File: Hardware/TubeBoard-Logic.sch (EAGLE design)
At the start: 35 parts, among them IC1 74HC373DW, IC2 74HC373DW, IC3 74HC85D, IC4 74HC04D, IC5 74HC08D, T1 MPSA42, T2 MPSA42

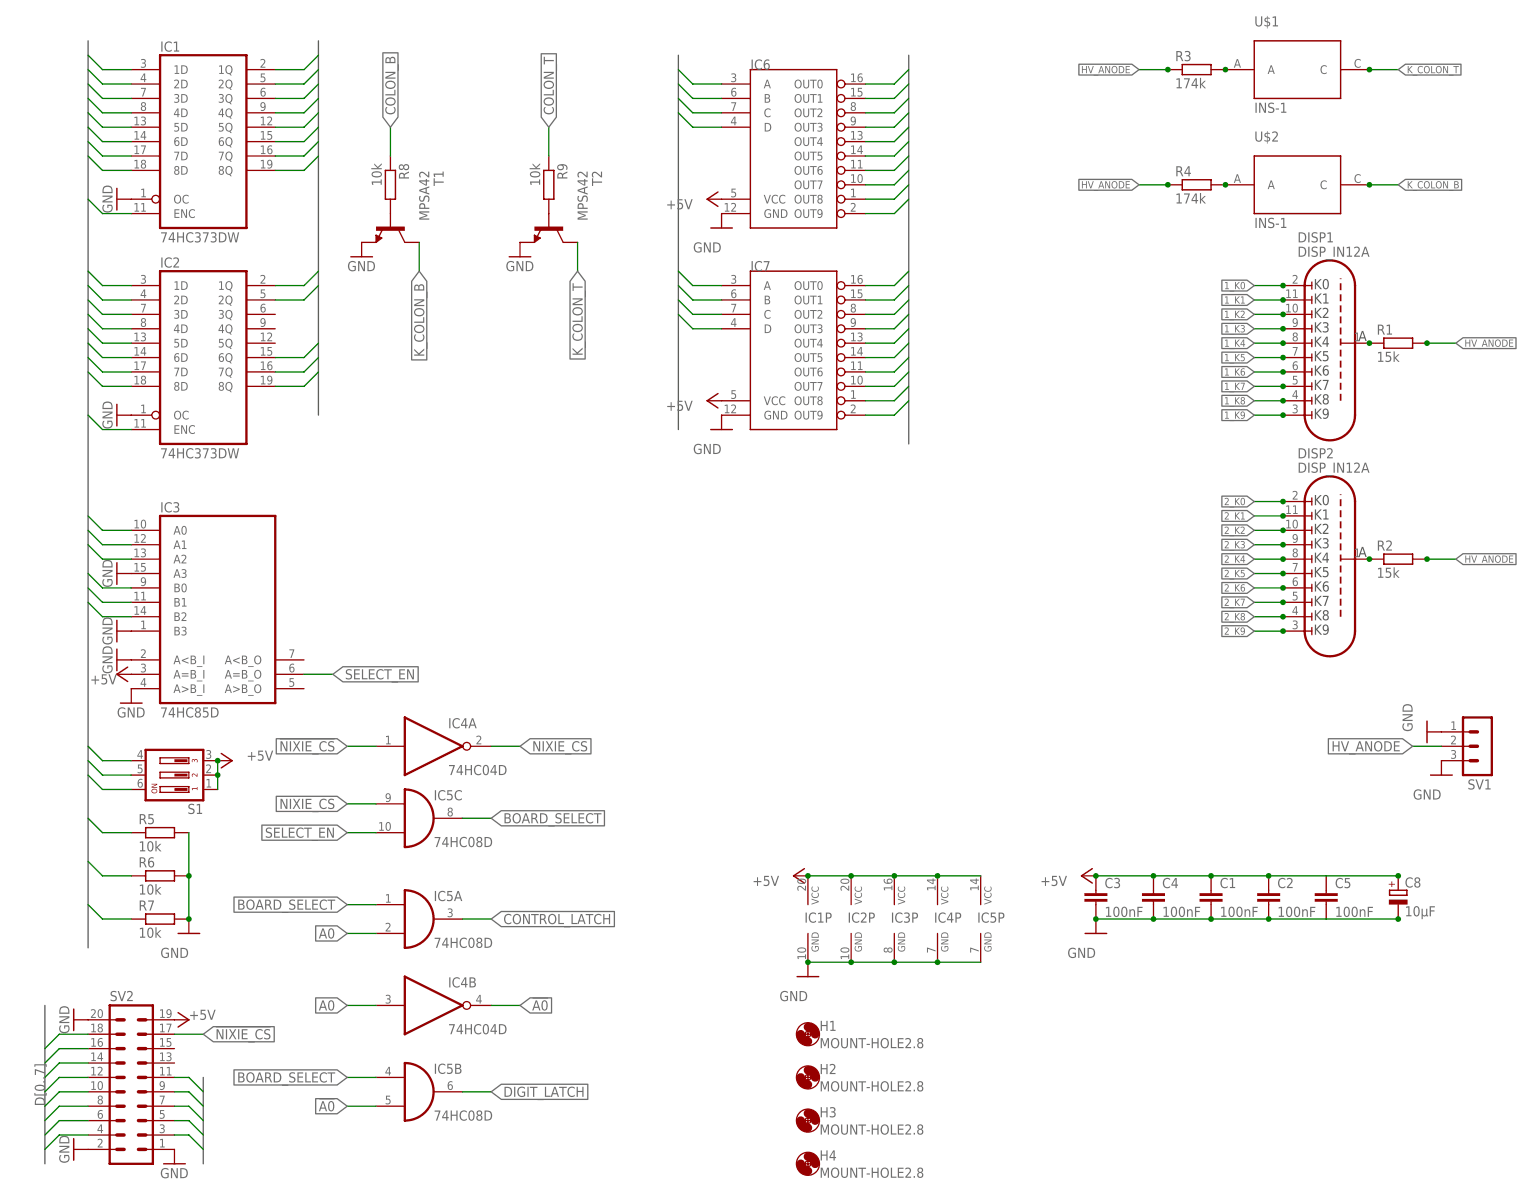
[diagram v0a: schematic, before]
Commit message: separated tubes and logic on two separate boards
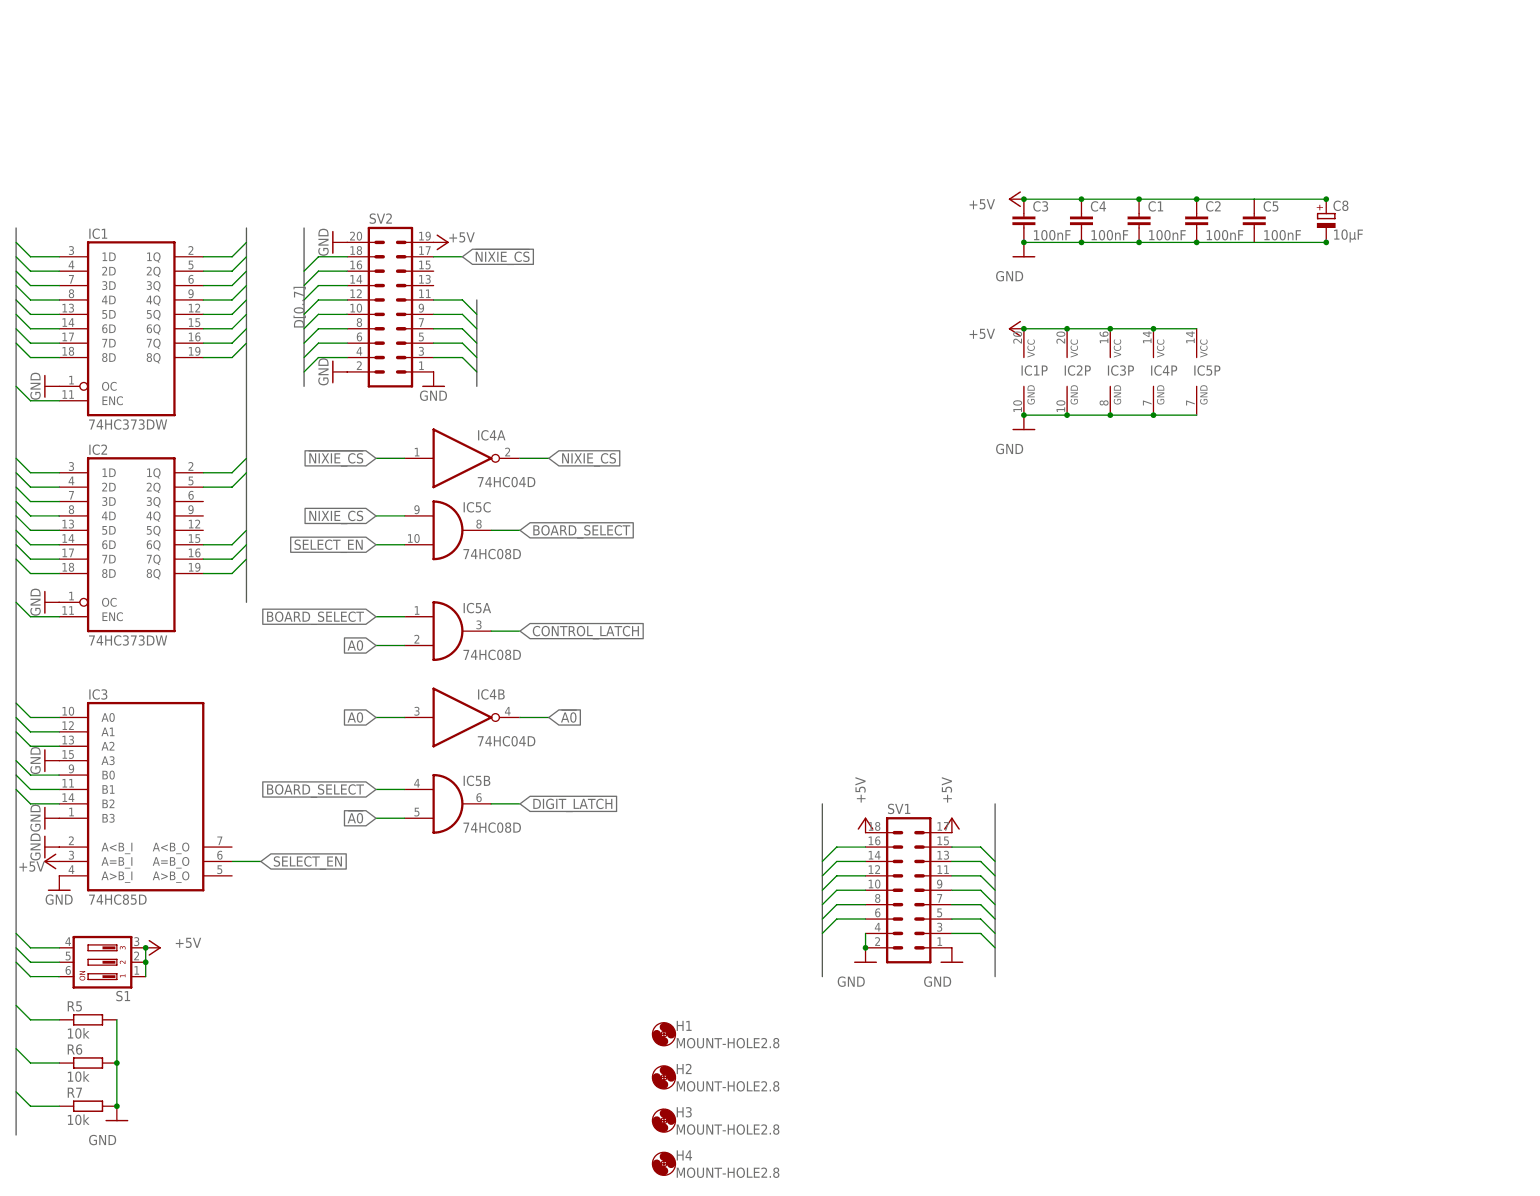
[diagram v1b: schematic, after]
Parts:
- removed DISP1, DISP2: DISP_IN12A, dp_devices:DISP_IN12A
- removed IC6, IC7: (no value), Parts:7441DIL16
- removed R1, R2: 15k, rcl:R-EU_0411/12
- removed R3, R4: 174k, rcl:R-EU_M1206
- removed R8, R9: 10k, rcl:R-EU_R2012
- removed T1, T2: MPSA42, transistor:MPSA42-NPN-TO92-EBC
- removed U$1, U$2: INS-1, Parts:INS-1
- SV1: device con-lstb:MA03-1 -> con-lstb:MA09-2
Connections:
- removed net 1_K0: DISP1.K0, IC6.OUT0
- removed net 1_K1: DISP1.K1, IC6.OUT1
- removed net 1_K2: DISP1.K2, IC6.OUT2
- removed net 1_K3: DISP1.K3, IC6.OUT3
- removed net 1_K4: DISP1.K4, IC6.OUT4
- removed net 1_K5: DISP1.K5, IC6.OUT5
- removed net 1_K6: DISP1.K6, IC6.OUT6
- removed net 1_K7: DISP1.K7, IC6.OUT7
- removed net 1_K8: DISP1.K8, IC6.OUT8
- removed net 1_K9: DISP1.K9, IC6.OUT9
- removed net 2_K0: DISP2.K0, IC7.OUT0
- removed net 2_K1: DISP2.K1, IC7.OUT1
- removed net 2_K2: DISP2.K2, IC7.OUT2
- removed net 2_K3: DISP2.K3, IC7.OUT3
- removed net 2_K4: DISP2.K4, IC7.OUT4
- removed net 2_K5: DISP2.K5, IC7.OUT5
- removed net 2_K6: DISP2.K6, IC7.OUT6
- removed net 2_K7: DISP2.K7, IC7.OUT7
- removed net 2_K8: DISP2.K8, IC7.OUT8
- removed net 2_K9: DISP2.K9, IC7.OUT9
- removed net HV_ANODE: R1.2, R2.2, R3.1, R4.1, SV1.2
- removed net K_COLON_B: T1.C, U$2.C
- removed net K_COLON_T: T2.C, U$1.C
- removed net N$1: DISP1.ANODE, R1.1
- removed net N$2: DISP2.ANODE, R2.1
- removed net N$3: R3.2, U$1.A
- removed net N$4: R4.2, U$2.A
- removed net N$5: R8.2, T1.B
- removed net N$6: R9.2, T2.B
- net +5V: now also SV1.17, SV1.18; no longer IC6.VCC, IC7.VCC
- net COLON_B: now also SV1.8; no longer R8.1
- net COLON_T: now also SV1.6; no longer R9.1
- net DRIVE_HI: now also SV1.3
- net DRIVE_LO: now also SV1.7
- net DRIVE_MED: now also SV1.5
- net GND: now also SV1.2, SV1.4; no longer IC6.GND, IC7.GND, SV1.3, T1.E, T2.E
- net LDIGIT0: now also SV1.16; no longer IC6.A
- net LDIGIT1: now also SV1.14; no longer IC6.B
- net LDIGIT2: now also SV1.12; no longer IC6.C
- net LDIGIT3: now also SV1.10; no longer IC6.D
- net RDIGIT0: now also SV1.15; no longer IC7.A
- net RDIGIT1: now also SV1.13; no longer IC7.B
- net RDIGIT2: now also SV1.11; no longer IC7.C
- net RDIGIT3: now also SV1.9; no longer IC7.D
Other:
- moved on the sheet: C1, C2, C3, C4, C5, C8, H1, H2, H3, H4, IC1, IC1P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

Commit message: routed tube logic board
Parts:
- added SV3: (no value), con-lstb:MA10-2
- added WEED1: WEED, Parts:WEED
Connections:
- net !NIXIE_CS: now also SV3.17
- net +5V: now also SV3.19
- net A0: now also SV3.3
- net A1: now also SV3.5
- net A2: now also SV3.7
- net A3: now also SV3.9
- net A4: now also SV3.11
- net D0: now also SV3.8
- net D1: now also SV3.6
- net D2: now also SV3.4
- net D3: now also SV3.10
- net D4: now also SV3.12
- net D5: now also SV3.14
- net D6: now also SV3.16
- net D7: now also SV3.18
- net GND: now also SV3.1, SV3.2, SV3.20
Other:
- moved on the sheet: SV2

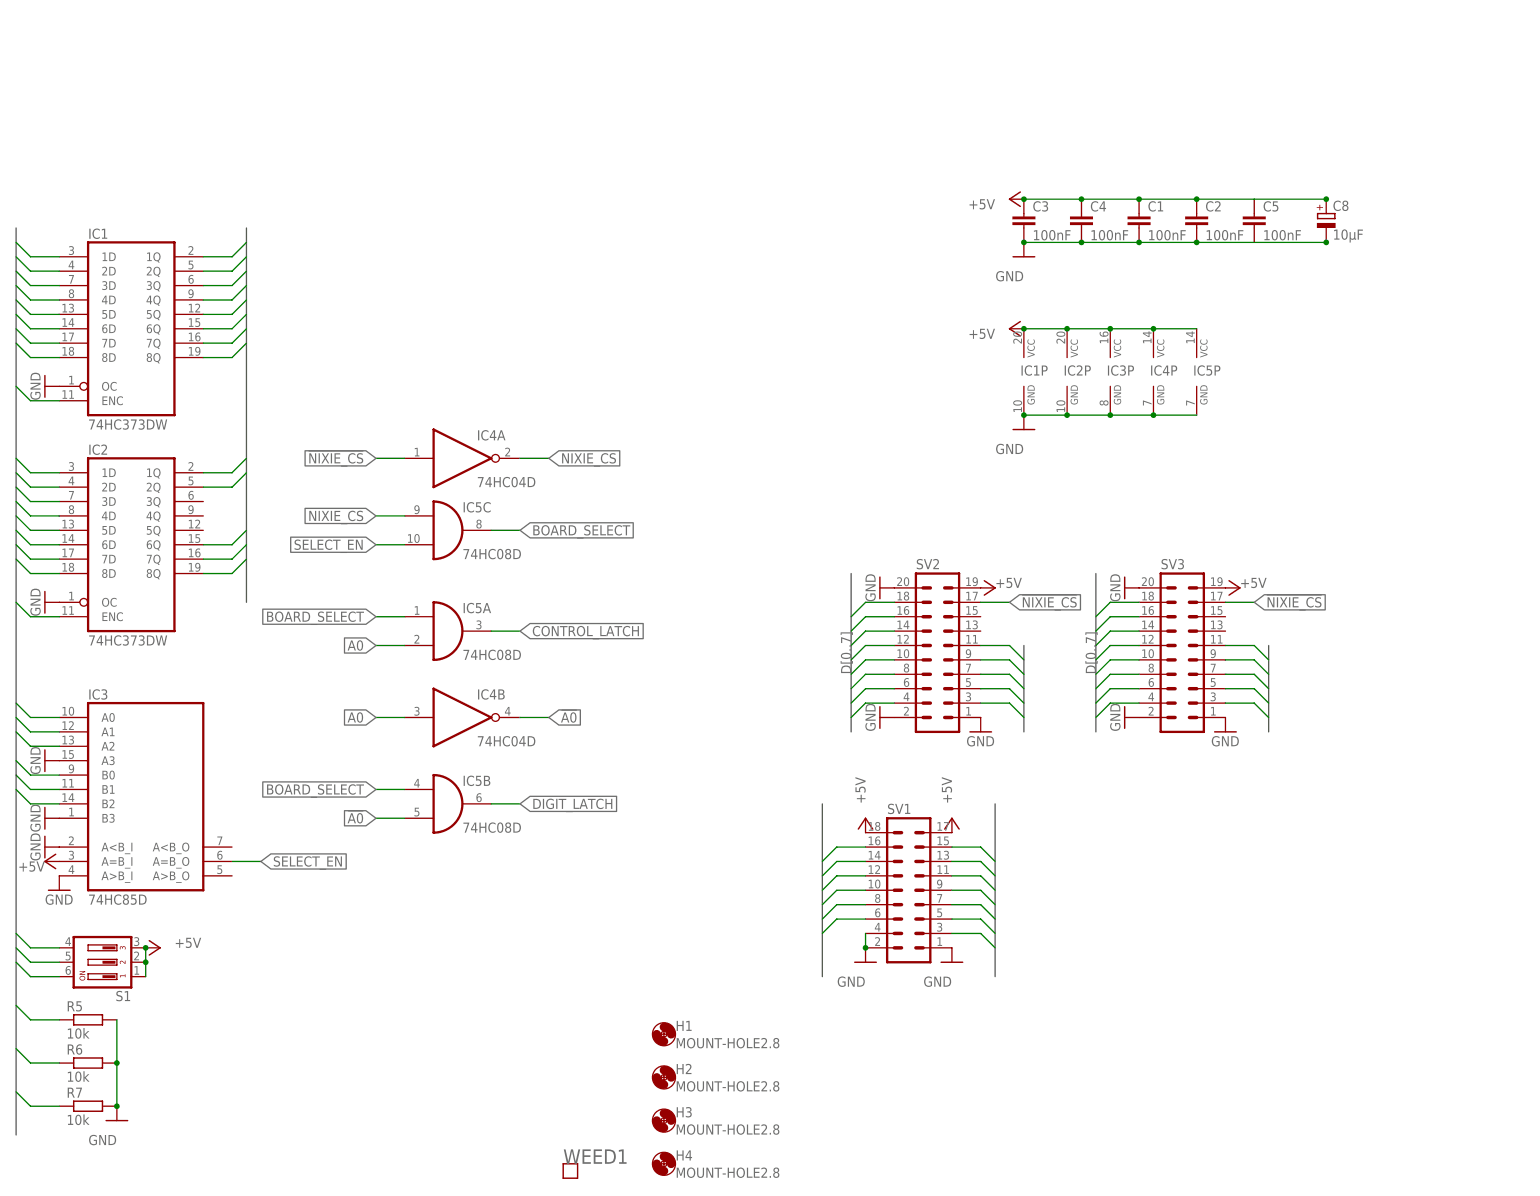
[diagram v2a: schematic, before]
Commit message: added data bus resistors; better reset circuit
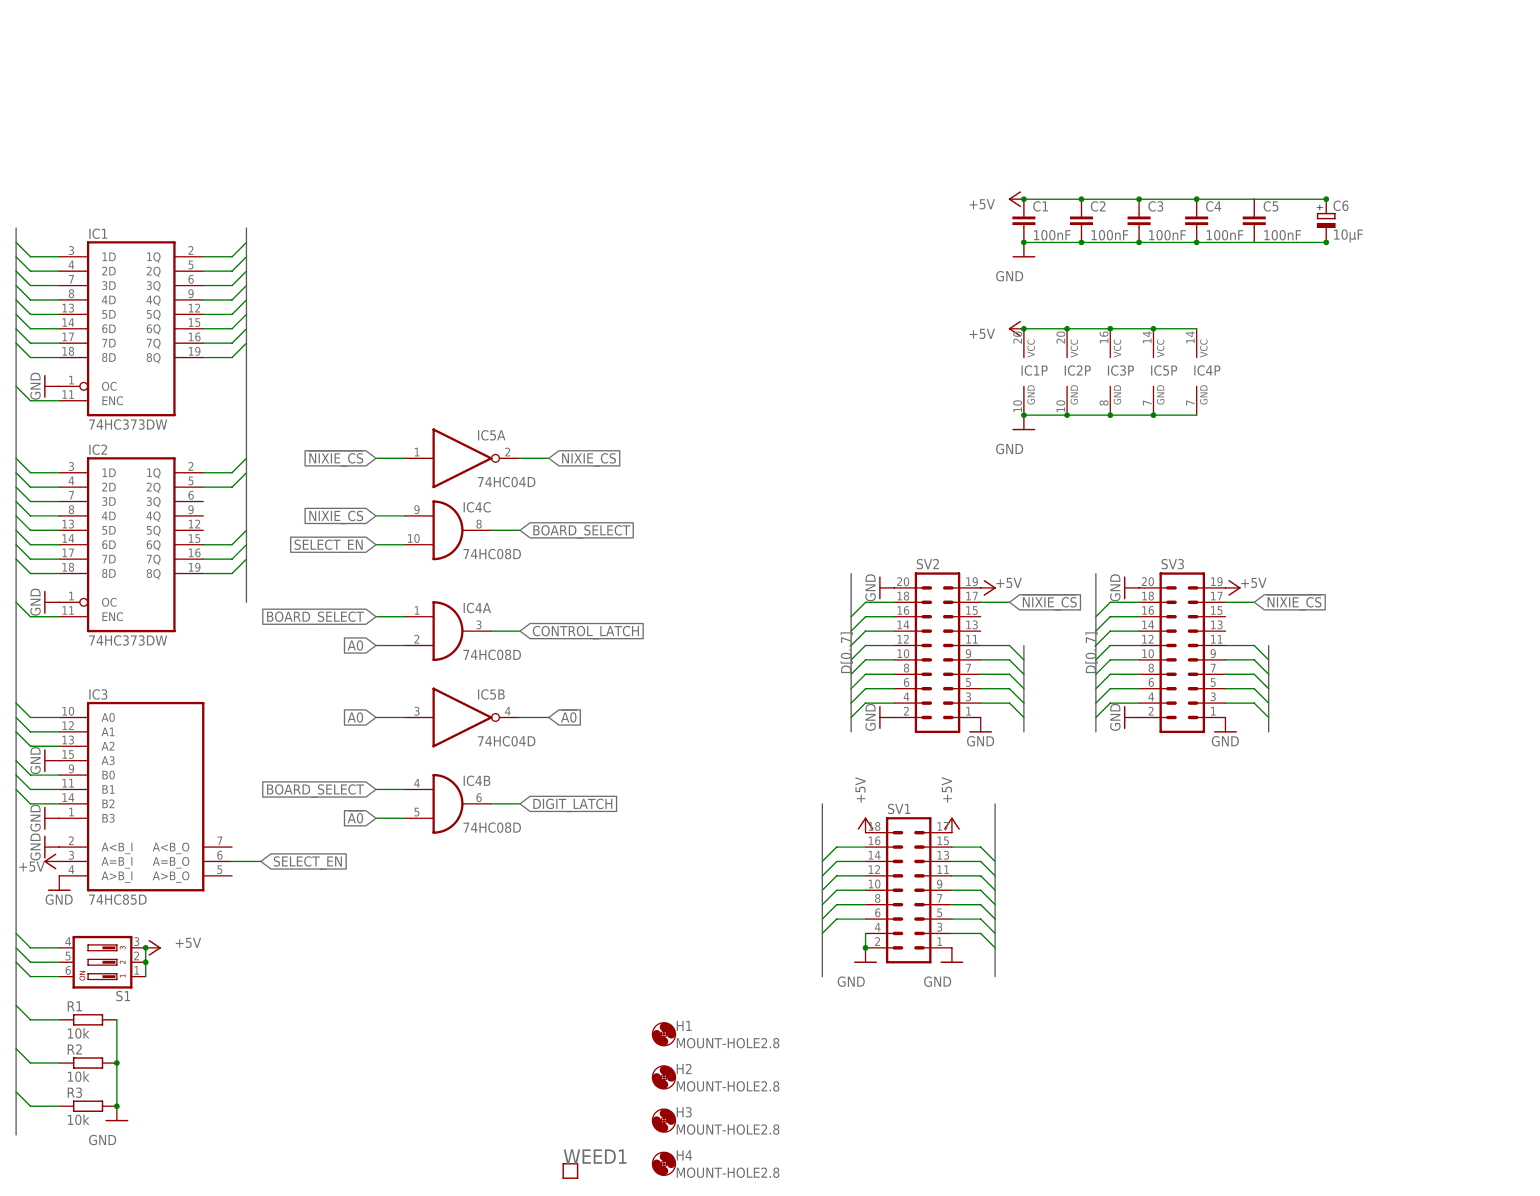
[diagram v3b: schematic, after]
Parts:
- IC4: value 74HC04D -> 74HC08D; device 74xx-eu:74HC04D -> 74xx-eu:74HC08D
- IC5: value 74HC08D -> 74HC04D; device 74xx-eu:74HC08D -> 74xx-eu:74HC04D
- renumbered C8 to C6, R5 to R1, R6 to R2, R7 to R3
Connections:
- net !A0: now also IC4B.I1, IC5B.O; no longer IC4B.O, IC5B.I1
- net !NIXIE_CS: now also IC5A.I; no longer IC4A.I
- net A0: now also IC4A.I1, IC5B.I; no longer IC4B.I, IC5A.I1
- net BOARD_SELECT: now also IC4A.I0, IC4B.I0, IC4C.O; no longer IC5A.I0, IC5B.I0, IC5C.O
- net CONTROL_LATCH: now also IC4A.O; no longer IC5A.O
- net DIGIT_LATCH: now also IC4B.O; no longer IC5B.O
- net NIXIE_CS: now also IC4C.I0, IC5A.O; no longer IC4A.O, IC5C.I0
- net SELECT_EN: now also IC4C.I1; no longer IC5C.I1
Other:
- moved on the sheet: C1, C2, C3, C4, IC4A, IC4B, IC4P, IC5A, IC5B, IC5P

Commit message: tied unused logic on tube board logic board to ground
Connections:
- net GND: now also IC4D.I0, IC4D.I1, IC5C.I, IC5D.I, IC5E.I, IC5F.I
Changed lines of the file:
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@@
 <part name="GND17" library="supply1" library_urn="urn:adsk.eagle:library:371" deviceset="GND" device=""/>
 <part name="WEED1" library="Parts" deviceset="WEED" device=""/>
+<part name="FRAME2" library="frames" library_urn="urn:adsk.eagle:library:229" deviceset="LETTER_L" device=""/>
+<part name="GND18" library="supply1" library_urn="urn:adsk.eagle:library:371" deviceset="GND" device=""/>
+<part name="GND19" library="supply1" library_urn="urn:adsk.eagle:library:371" deviceset="GND" device=""/>
 </parts>
 <sheets>
@@
 </segment>
 </net>
+</nets>
+</sheet>
+<sheet>
+<plain>
+</plain>
+<instances>
+<instance part="FRAME2" gate="G$1" x="0" y="0" smashed="yes"/>
+<instance part="FRAME2" gate="G$2" x="147.32" y="0" smashed="yes">
+<attribute name="LAST_DATE_TIME" x="160.02" y="1.27" size="2.54" layer="94"/>
+<attribute name="SHEET" x="233.68" y="1.27" size="2.54" layer="94"/>
+<attribute name="DRAWING_NAME" x="165.1" y="19.05" size="2.54" layer="94"/>
+</instance>
+<instance part="IC5" gate="C" x="20.32" y="175.26" smashed="yes">
+<attribute name="NAME" x="22.86" y="178.435" size="1.778" layer="95"/>
+<attribute name="VALUE" x="22.86" y="170.18" size="1.778" layer="96"/>
+</instance>
+<instance part="IC5" gate="D" x="20.32" y="160.02" smashed="yes">
+<attribute name="NAME" x="22.86" y="163.195" size="1.778" layer="95"/>
+<attribute name="VALUE" x="22.86" y="154.94" size="1.778" layer="96"/>
+</instance>
+<instance part="IC5" gate="E" x="20.32" y="144.78" smashed="yes">
+<attribute name="NAME" x="22.86" y="147.955" size="1.778" layer="95"/>
+<attribute name="VALUE" x="22.86" y="139.7" size="1.778" layer="96"/>
+</instance>
+<instance part="IC5" gate="F" x="20.32" y="129.54" smashed="yes">
+<attribute name="NAME" x="22.86" y="132.715" size="1.778" layer="95"/>
+<attribute name="VALUE" x="22.86" y="124.46" size="1.778" layer="96"/>
+</instance>
+<instance part="GND18" gate="1" x="10.16" y="127" smashed="yes">
+<attribute name="VALUE" x="7.62" y="124.46" size="1.778" layer="96"/>
+</instance>
+<instance part="IC4" gate="D" x="58.42" y="172.72" smashed="yes">
+<attribute name="NAME" x="60.96" y="175.895" size="1.778" layer="95"/>
+<attribute name="VALUE" x="60.96" y="167.64" size="1.778" layer="96"/>
+</instance>
+<instance part="GND19" gate="1" x="50.8" y="167.64" smashed="yes">
+<attribute name="VALUE" x="48.26" y="165.1" size="1.778" layer="96"/>
+</instance>
+</instances>
+<busses>
+</busses>
+<nets>
+<net name="GND" class="0">
+<segment>
+<pinref part="IC5" gate="C" pin="I"/>
+<pinref part="IC5" gate="F" pin="I"/>
+<wire x1="10.16" y1="175.26" x2="10.16" y2="160.02" width="0.1524" layer="91"/>
+<pinref part="IC5" gate="D" pin="I"/>
+<wire x1="10.16" y1="160.02" x2="10.16" y2="144.78" width="0.1524" layer="91"/>
+<junction x="10.16" y="160.02"/>
+<pinref part="IC5" gate="E" pin="I"/>
+<wire x1="10.16" y1="144.78" x2="10.16" y2="129.54" width="0.1524" layer="91"/>
+<junction x="10.16" y="144.78"/>
+<pinref part="GND18" gate="1" pin="GND"/>
+<junction x="10.16" y="129.54"/>
+</segment>
+<segment>
+<pinref part="IC4" gate="D" pin="I0"/>
+<pinref part="IC4" gate="D" pin="I1"/>
+<wire x1="50.8" y1="175.26" x2="50.8" y2="170.18" width="0.1524" layer="91"/>
+<pinref part="GND19" gate="1" pin="GND"/>
+<junction x="50.8" y="170.18"/>
+</segment>
+</net>
